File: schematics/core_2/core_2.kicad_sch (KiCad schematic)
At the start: 23 parts, among them U1 74LS04, U2 74LS574, U3 74LS02, U5 74LS00

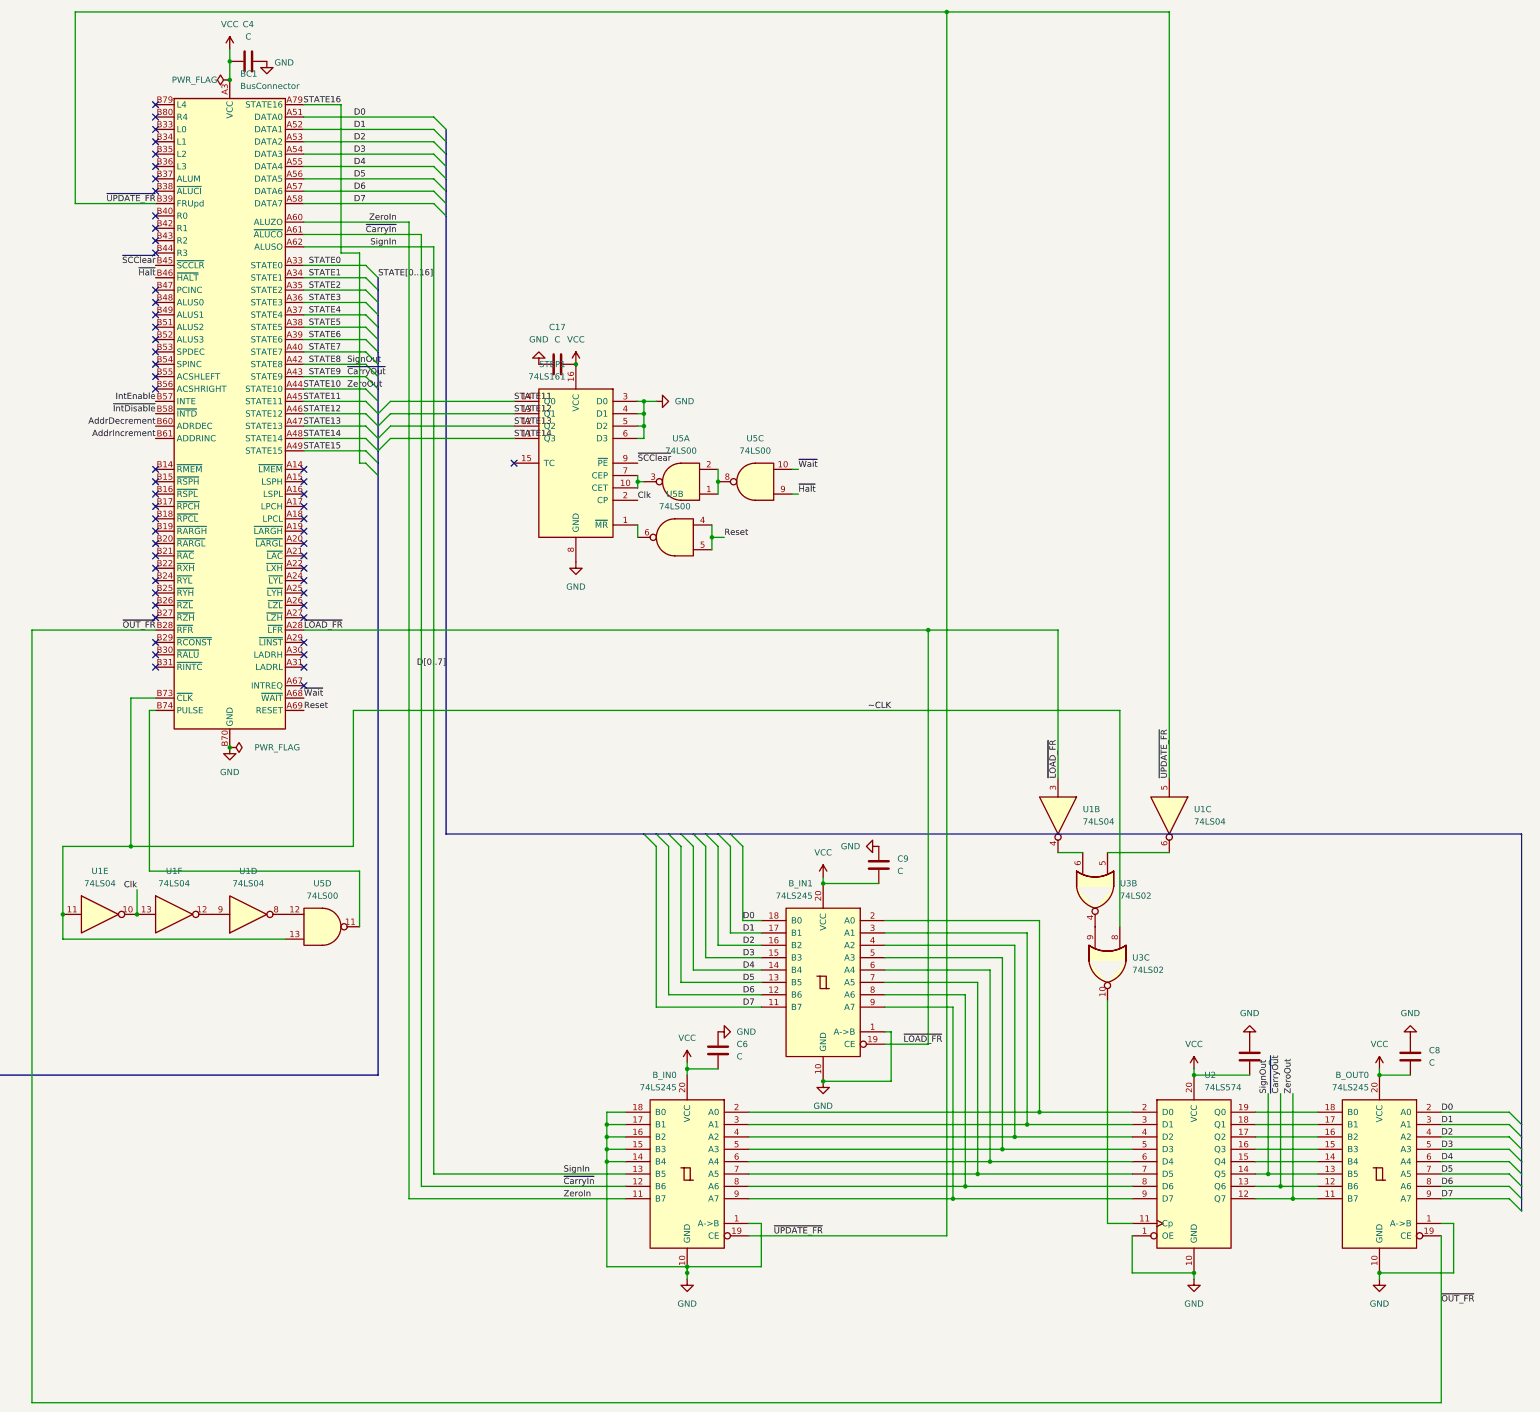
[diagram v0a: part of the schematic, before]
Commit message: added testpoints on core 2
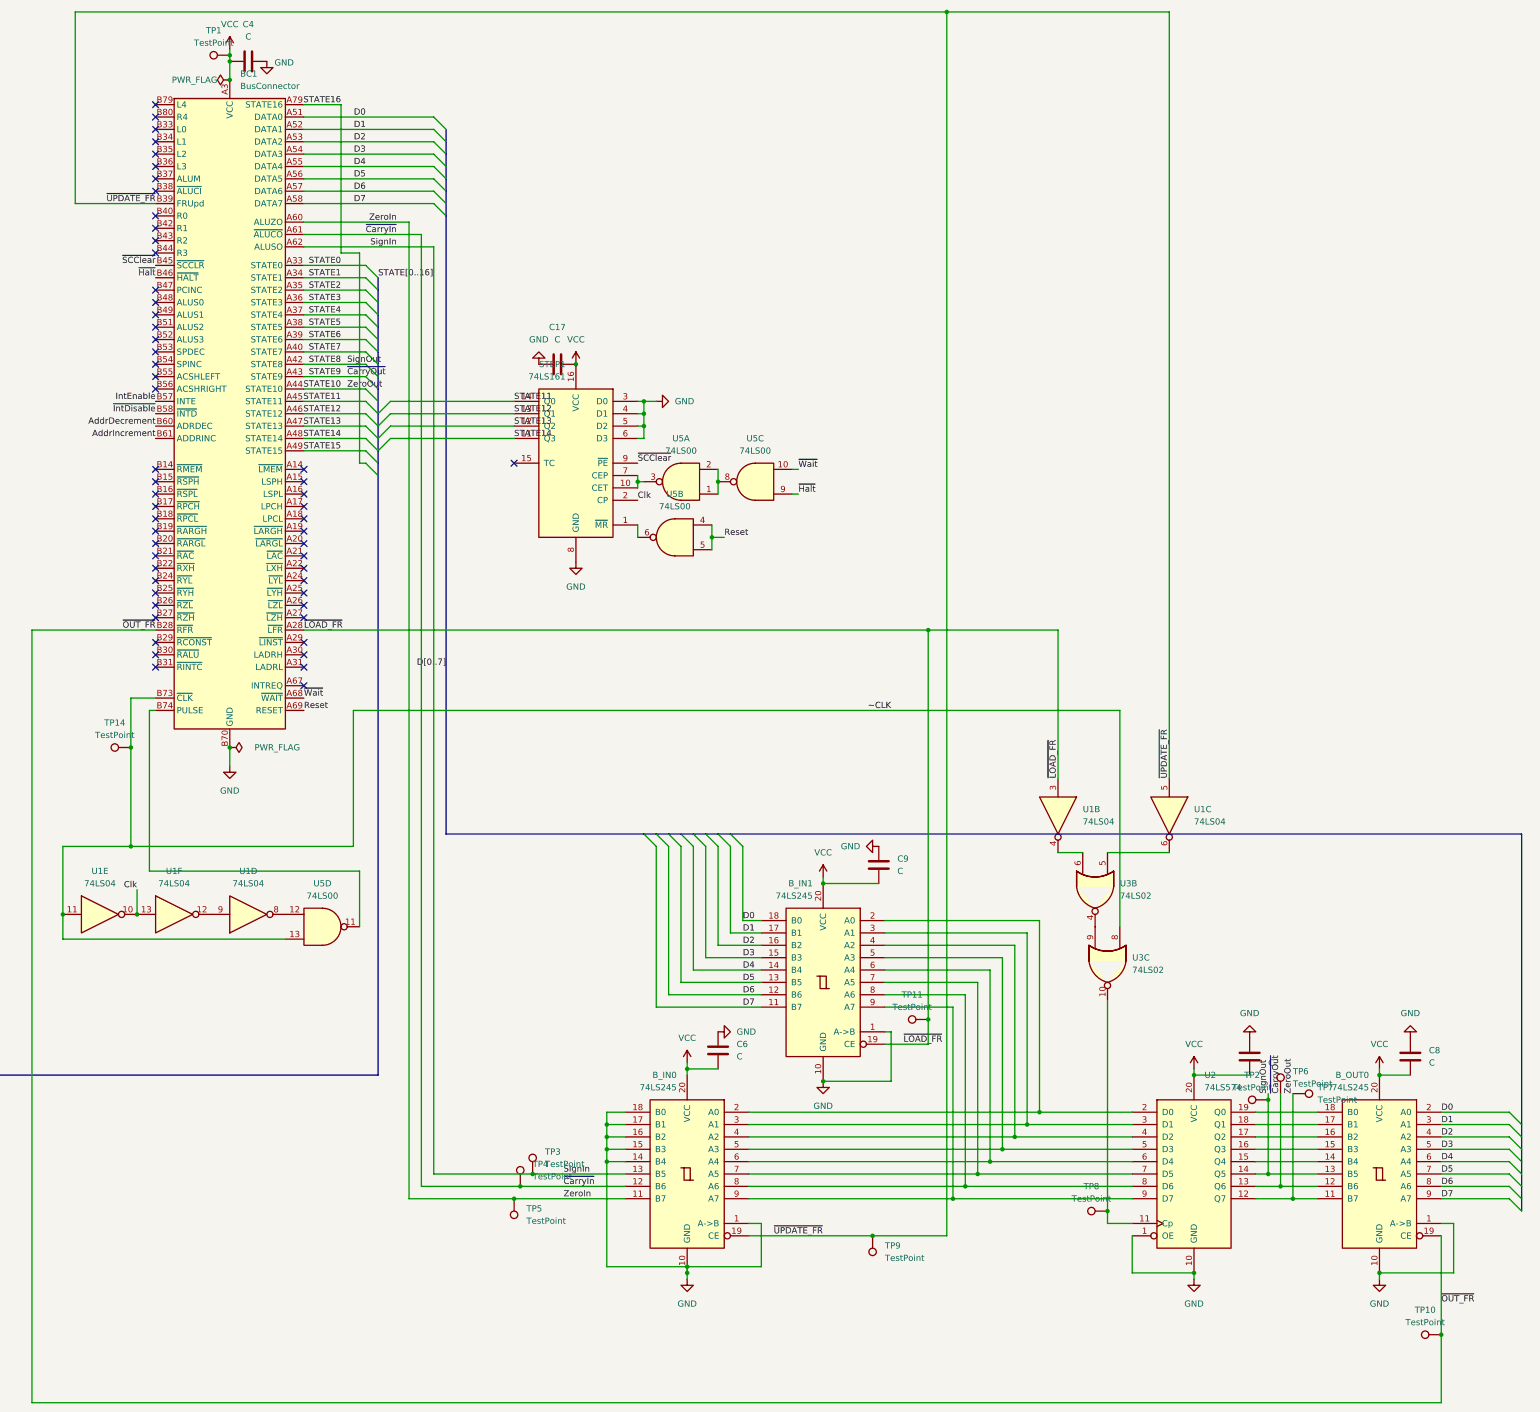
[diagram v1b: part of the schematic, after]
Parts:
- added TP1, TP10, TP11, TP14, TP2, TP3, TP4, TP5, TP6, TP7, TP8, TP9: TestPoint, TestPoint:TestPoint_Pad_D1.0mm, symbol Connector:TestPoint
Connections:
- net STATE10: now also TP7.1
- net STATE8: now also TP2.1
- net STATE9: now also TP6.1
- net SignIn: now also TP3.1
- net VCC: now also TP1.1
- net ZeroIn: now also TP5.1
- net ~CLK: now also TP14.1
- net ~{CarryIn}: now also TP4.1
- net ~{LOAD_FR}: now also TP11.1
- net ~{OUT_FR}: now also TP10.1
- net ~{UPDATE_FR}: now also TP9.1
- net at U2.11 (Cp), U3.10: now also TP8.1

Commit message: fix
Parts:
- renumbered TP6 to CarryO1, TP1 to PWR1, TP2 to SignO1, TP5 to ZerroIn1, TP7 to ZerroO1, TP14 to ~{CLK}1, TP4 to ~{CarrIn}1, TP8 to ~{ENBL}1, TP11 to ~{L_FR}1, TP10 to ~{OUT_FR}1, TP3 to ~{SignIn}1, TP9 to ~{UPD_FR}1
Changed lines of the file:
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@@
 		(on_board yes)
 		(dnp no)
-		(fields_autoplaced yes)
-		(property "Reference" "TP3"
+		(property "Reference" "~{SignIn}1"
 			(at 280.67 279.9079 0)
 			(effects
@@
 			(project ""
 				(path "/59b2db81-41fa-4862-96ef-fb4ce3ab7be6"
-					(reference "TP3")
+					(reference "~{SignIn}1")
 					(unit 1)
 				)
@@
 		(on_board yes)
 		(dnp no)
-		(fields_autoplaced yes)
-		(property "Reference" "TP7"
-			(at 439.42 266.6999 90)
+		(property "Reference" "ZerroO1"
+			(at 435.102 270.002 90)
 			(effects
 				(font
@@
 			(project "core_2"
 				(path "/59b2db81-41fa-4862-96ef-fb4ce3ab7be6"
-					(reference "TP7")
+					(reference "ZerroO1")
 					(unit 1)
 				)
@@
 		(dnp no)
 		(fields_autoplaced yes)
-		(property "Reference" "TP1"
+		(property "Reference" "PWR1"
 			(at 212.598 49.53 90)
 			(effects
@@
 			(project ""
 				(path "/59b2db81-41fa-4862-96ef-fb4ce3ab7be6"
-					(reference "TP1")
+					(reference "PWR1")
 					(unit 1)
 				)
@@
 		(dnp no)
 		(fields_autoplaced yes)
-		(property "Reference" "TP8"
+		(property "Reference" "~{ENBL}1"
 			(at 392.938 287.02 90)
 			(effects
@@
 			(project "core_2"
 				(path "/59b2db81-41fa-4862-96ef-fb4ce3ab7be6"
-					(reference "TP8")
+					(reference "~{ENBL}1")
 					(unit 1)
 				)
@@
 		(dnp no)
 		(fields_autoplaced yes)
-		(property "Reference" "TP11"
+		(property "Reference" "~{L_FR}1"
 			(at 356.108 247.65 90)
 			(effects
@@
 			(project "core_2"
 				(path "/59b2db81-41fa-4862-96ef-fb4ce3ab7be6"
-					(reference "TP11")
+					(reference "~{L_FR}1")
 					(unit 1)
 				)
@@
 		(on_board yes)
 		(dnp no)
-		(fields_autoplaced yes)
-		(property "Reference" "TP6"
+		(property "Reference" "CarryO1"
 			(at 434.34 263.3979 0)
 			(effects
@@
 			(project "core_2"
 				(path "/59b2db81-41fa-4862-96ef-fb4ce3ab7be6"
-					(reference "TP6")
+					(reference "CarryO1")
 					(unit 1)
 				)
@@
 		(dnp no)
 		(fields_autoplaced yes)
-		(property "Reference" "TP9"
+		(property "Reference" "~{UPD_FR}1"
 			(at 350.52 299.2119 0)
 			(effects
@@
 			(project "core_2"
 				(path "/59b2db81-41fa-4862-96ef-fb4ce3ab7be6"
-					(reference "TP9")
+					(reference "~{UPD_FR}1")
 					(unit 1)
 				)
@@
 		(on_board yes)
 		(dnp no)
-		(fields_autoplaced yes)
-		(property "Reference" "TP2"
-			(at 425.958 264.16 90)
+		(property "Reference" "SignO1"
+			(at 425.704 264.668 90)
 			(effects
 				(font
@@
 			(project "core_2"
 				(path "/59b2db81-41fa-4862-96ef-fb4ce3ab7be6"
-					(reference "TP2")
+					(reference "SignO1")
 					(unit 1)
 				)
@@
 		(on_board yes)
 		(dnp no)
-		(fields_autoplaced yes)
-		(property "Reference" "TP4"
-			(at 278.13 282.4479 0)
+		(property "Reference" "~{CarrIn}1"
+			(at 270.51 285.75 0)
 			(effects
 				(font
@@
 			(project "core_2"
 				(path "/59b2db81-41fa-4862-96ef-fb4ce3ab7be6"
-					(reference "TP4")
+					(reference "~{CarrIn}1")
 					(unit 1)
 				)
@@
 		(dnp no)
 		(fields_autoplaced yes)
-		(property "Reference" "TP5"
+		(property "Reference" "ZerroIn1"
 			(at 276.86 291.5919 0)
 			(effects
@@
 			(project "core_2"
 				(path "/59b2db81-41fa-4862-96ef-fb4ce3ab7be6"
-					(reference "TP5")
+					(reference "ZerroIn1")
 					(unit 1)
 				)
@@
 		(dnp no)
 		(fields_autoplaced yes)
-		(property "Reference" "TP10"
+		(property "Reference" "~{OUT_FR}1"
 			(at 461.518 312.42 90)
 			(effects
@@
 			(project "core_2"
 				(path "/59b2db81-41fa-4862-96ef-fb4ce3ab7be6"
-					(reference "TP10")
+					(reference "~{OUT_FR}1")
 					(unit 1)
 				)
@@
 		(dnp no)
 		(fields_autoplaced yes)
-		(property "Reference" "TP14"
+		(property "Reference" "~{CLK}1"
 			(at 192.278 191.77 90)
 			(effects
@@
 			(project "core_2"
 				(path "/59b2db81-41fa-4862-96ef-fb4ce3ab7be6"
-					(reference "TP14")
+					(reference "~{CLK}1")
 					(unit 1)
 				)

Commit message: Push periphery and fix schematics
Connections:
- net GND: no longer TABLE7.27 (~{WE}), TABLE8.27 (~{WE})
- net VCC: now also TABLE7.27 (~{WE}), TABLE8.27 (~{WE})
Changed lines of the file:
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@@
+	(symbol
+		(lib_id "power:VCC")
+		(at 105.41 238.76 0)
+		(unit 1)
+		(exclude_from_sim no)
+		(in_bom yes)
+		(on_board yes)
+		(dnp no)
+		(property "Reference" "#PWR09"
+			(at 105.41 242.57 0)
+			(effects
+				(font
+					(size 1.27 1.27)
+				)
+				(hide yes)
+			)
+		)
+		(property "Value" "VCC"
+			(at 105.41 233.68 0)
+			(effects
+				(font
+					(size 1.27 1.27)
+				)
+			)
+		)
+		(property "Footprint" ""
+			(at 105.41 238.76 0)
+			(effects
+				(font
+					(size 1.27 1.27)
+				)
+				(hide yes)
+			)
+		)
+		(property "Datasheet" ""
+			(at 105.41 238.76 0)
+			(effects
+				(font
+					(size 1.27 1.27)
+				)
+				(hide yes)
+			)
+		)
+		(property "Description" "Power symbol creates a global label with name \"VCC\""
+			(at 105.41 238.76 0)
+			(effects
+				(font
+					(size 1.27 1.27)
+				)
+				(hide yes)
+			)
+		)
+		(pin "1"
+		)
+		(instances
+			(project "core_2"
+				(path "/59b2db81-41fa-4862-96ef-fb4ce3ab7be6"
+					(reference "#PWR09")
+					(unit 1)
+				)
+			)
+		)
+	)
 	(symbol
 		(lib_id "power:VCC")
@@
 	)
 	(symbol
+		(lib_id "power:VCC")
+		(at 105.41 172.72 0)
+		(unit 1)
+		(exclude_from_sim no)
+		(in_bom yes)
+		(on_board yes)
+		(dnp no)
+		(property "Reference" "#PWR01"
+			(at 105.41 176.53 0)
+			(effects
+				(font
+					(size 1.27 1.27)
+				)
+				(hide yes)
+			)
+		)
+		(property "Value" "VCC"
+			(at 105.41 167.64 0)
+			(effects
+				(font
+					(size 1.27 1.27)
+				)
+			)
+		)
+		(property "Footprint" ""
+			(at 105.41 172.72 0)
+			(effects
+				(font
+					(size 1.27 1.27)
+				)
+				(hide yes)
+			)
+		)
+		(property "Datasheet" ""
+			(at 105.41 172.72 0)
+			(effects
+				(font
+					(size 1.27 1.27)
+				)
+				(hide yes)
+			)
+		)
+		(property "Description" "Power symbol creates a global label with name \"VCC\""
+			(at 105.41 172.72 0)
+			(effects
+				(font
+					(size 1.27 1.27)
+				)
+				(hide yes)
+			)
+		)
+		(pin "1"
+		)
+		(instances
+			(project "core_2"
+				(path "/59b2db81-41fa-4862-96ef-fb4ce3ab7be6"
+					(reference "#PWR01")
+					(unit 1)
+				)
+			)
+		)
+	)
+	(symbol
 		(lib_id "power:GND")
 		(at 105.41 177.8 270)
@@
 	)
 	(symbol
-		(lib_id "power:GND")
-		(at 105.41 172.72 270)
-		(unit 1)
-		(exclude_from_sim no)
-		(in_bom yes)
-		(on_board yes)
-		(dnp no)
-		(fields_autoplaced yes)
-		(property "Reference" "#PWR01"
-			(at 99.06 172.72 0)
-			(effects
-				(font
-					(size 1.27 1.27)
-				)
-				(hide yes)
-			)
-		)
-		(property "Value" "GND"
-			(at 101.6 172.7199 90)
-			(effects
-				(font
-					(size 1.27 1.27)
-				)
-				(justify right)
-			)
-		)
-		(property "Footprint" ""
-			(at 105.41 172.72 0)
-			(effects
-				(font
-					(size 1.27 1.27)
-				)
-				(hide yes)
-			)
-		)
-		(property "Datasheet" ""
-			(at 105.41 172.72 0)
-			(effects
-				(font
-					(size 1.27 1.27)
-				)
-				(hide yes)
-			)
-		)
-		(property "Description" "Power symbol creates a global label with name \"GND\" , ground"
-			(at 105.41 172.72 0)
-			(effects
-				(font
-					(size 1.27 1.27)
-				)
-				(hide yes)
-			)
-		)
-		(pin "1"
-		)
-		(instances
-			(project "core_2"
-				(path "/59b2db81-41fa-4862-96ef-fb4ce3ab7be6"
-					(reference "#PWR01")
-					(unit 1)
-				)
-			)
-		)
-	)
-	(symbol
 		(lib_id "power:VCC")
 		(at 499.11 269.24 0)
@@
 					(unit 1)
 				)
-			)
-		)
-	)
-	(symbol
-		(lib_id "power:GND")
-		(at 105.41 238.76 270)
-		(unit 1)
-		(exclude_from_sim no)
-		(in_bom yes)
-		(on_board yes)
-		(dnp no)
-		(fields_autoplaced yes)
-		(property "Reference" "#PWR09"
-			(at 99.06 238.76 0)
-			(effects
-				(font
-					(size 1.27 1.27)
-				)
-				(hide yes)
-			)
-		)
-		(property "Value" "GND"
-			(at 101.6 238.7599 90)
-			(effects
-				(font
-					(size 1.27 1.27)
-				)
-				(justify right)
-			)
-		)
-		(property "Footprint" ""
-			(at 105.41 238.76 0)
-			(effects
-				(font
-					(size 1.27 1.27)
-				)
-				(hide yes)
-			)
-		)
-		(property "Datasheet" ""
-			(at 105.41 238.76 0)
-			(effects
-				(font
-					(size 1.27 1.27)
-				)
-				(hide yes)
-			)
-		)
-		(property "Description" "Power symbol creates a global label with name \"GND\" , ground"
-			(at 105.41 238.76 0)
-			(effects
-				(font
-					(size 1.27 1.27)
-				)
-				(hide yes)
-			)
-		)
-		(pin "1"
-		)
-		(instances
-			(project "core_2"
-				(path "/59b2db81-41fa-4862-96ef-fb4ce3ab7be6"
-					(reference "#PWR09")
-					(unit 1)
-				)
